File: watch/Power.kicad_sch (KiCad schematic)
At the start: 17 parts, among them IC401 nPM1300-QEXX, X402 Battery

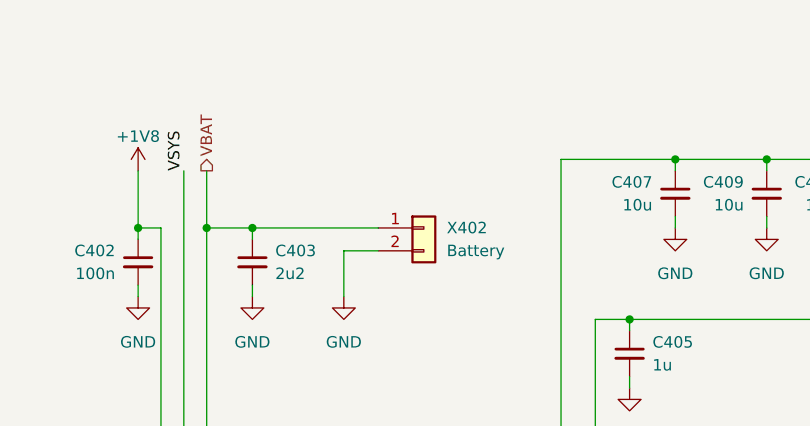
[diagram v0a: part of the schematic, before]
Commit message: Change to a larger battery connector (JST 1.25). Add pads for speaker instead.
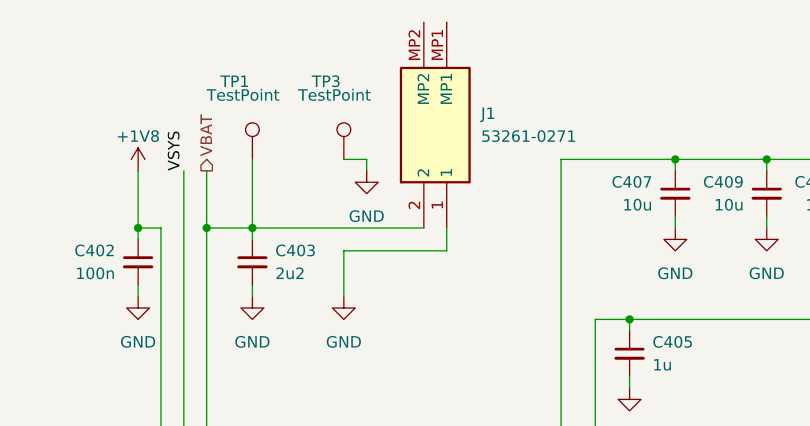
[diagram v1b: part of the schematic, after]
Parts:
- removed X402: Battery, JST_SH_SM02B-SRSS-TB_1x02-1MP_P1.00mm_Horizontal, symbol Connector_Generic:Conn_01x02
- added J1: 53261-0271, ZSWatch:molex_pico, symbol molex_pico:53261-0271
- added TP1, TP3: TestPoint, TestPoint:TestPoint_Loop_D3.50mm_Drill0.9mm_Beaded, symbol Connector:TestPoint
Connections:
- net GND: now also J1.1, TP3.1
- net VBAT: now also J1.2, TP1.1

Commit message: Fix BOM fields, optional speaker flags and connector 3D model
- Rename J1 fields to match the BOM generator
- Exclude optional LS801 from the board and BOM
- Correct the Molex footprint's 3D model reference
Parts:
- J1: Manufacturer_Name Molex -> (none); Manufacturer_Part_Number 53261-0271 -> (none); Mouser Part Number 538-53261-0271 -> (none); manf (none) -> Molex; manf# (none) -> 53261-0271; mouser# (none) -> 538-53261-0271
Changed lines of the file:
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@@
 			)
 		)
-		(property "Mouser Part Number" "538-53261-0271"
+		(property "mouser#" "538-53261-0271"
 			(at 693.04 17.78 0)
 			(effects
@@
 			)
 		)
-		(property "Manufacturer_Name" "Molex"
+		(property "manf" "Molex"
 			(at 893.04 17.78 0)
 			(effects
@@
 			)
 		)
-		(property "Manufacturer_Part_Number" "53261-0271"
+		(property "manf#" "53261-0271"
 			(at 993.04 17.78 0)
 			(effects

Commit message: Make battery/speaker stickout 0.5mm shorter. Add few extra Test Points for power at bottom.
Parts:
- added TP4, TP5, TP6: TestPoint, TestPoint:TestPoint_Pad_D1.0mm, symbol Connector:TestPoint
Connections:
- net +1V8: now also TP4.1
- net +3V0: now also TP5.1
- net VSYS: now also TP6.1
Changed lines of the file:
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@@
 	)
 	(junction
+		(at 252.73 29.21)
+		(diameter 0)
+		(color 0 0 0 0)
+	)
+	(junction
 		(at 231.14 83.82)
 		(diameter 0)
@@
 	)
 	(junction
+		(at 242.57 83.82)
+		(diameter 0)
+		(color 0 0 0 0)
+	)
+	(junction
 		(at 231.14 123.19)
 		(diameter 0)
@@
 		(color 0 0 0 0)
 	)
+	(junction
+		(at 242.57 101.6)
+		(diameter 0)
+		(color 0 0 0 0)
+	)
 	(no_connect
 		(at 137.16 96.52)
@@
 	(wire
 		(pts
+			(xy 242.57 83.82) (xy 251.46 83.82)
+		)
+		(stroke
+			(width 0)
+			(type default)
+		)
+	)
+	(wire
+		(pts
 			(xy 207.01 109.22) (xy 222.25 109.22)
 		)
@@
 	(wire
 		(pts
-			(xy 231.14 83.82) (xy 251.46 83.82)
+			(xy 231.14 83.82) (xy 242.57 83.82)
 		)
 		(stroke
@@
 	(wire
 		(pts
+			(xy 242.57 101.6) (xy 251.46 101.6)
+		)
+		(stroke
+			(width 0)
+			(type default)
+		)
+	)
+	(wire
+		(pts
 			(xy 226.06 29.21) (xy 213.36 29.21)
 		)
@@
 	(wire
 		(pts
-			(xy 246.38 29.21) (xy 264.16 29.21)
+			(xy 246.38 29.21) (xy 252.73 29.21)
 		)
 		(stroke
@@
 	(wire
 		(pts
-			(xy 222.25 101.6) (xy 251.46 101.6)
+			(xy 222.25 101.6) (xy 242.57 101.6)
 		)
 		(stroke
@@
 	(wire
 		(pts
+			(xy 252.73 29.21) (xy 264.16 29.21)
+		)
+		(stroke
+			(width 0)
+			(type default)
+		)
+	)
+	(wire
+		(pts
 			(xy 231.14 121.92) (xy 231.14 123.19)
 		)
@@
 	)
 	(symbol
+		(lib_id "Connector:TestPoint")
+		(at 252.73 29.21 0)
+		(unit 1)
+		(exclude_from_sim no)
+		(in_bom yes)
+		(on_board yes)
+		(dnp no)
+		(property "Reference" "TP6"
+			(at 249.174 20.574 0)
+			(effects
+				(font
+					(size 1.27 1.27)
+				)
+				(justify left)
+			)
+		)
+		(property "Value" "TestPoint"
+			(at 247.65 22.098 0)
+			(effects
+				(font
+					(size 1.27 1.27)
+				)
+				(justify left)
+			)
+		)
+		(property "Footprint" "TestPoint:TestPoint_Pad_D1.0mm"
+			(at 257.81 29.21 0)
+			(effects
+				(font
+					(size 1.27 1.27)
+				)
+				(hide yes)
+			)
+		)
+		(property "Datasheet" "~"
+			(at 257.81 29.21 0)
+			(effects
+				(font
+					(size 1.27 1.27)
+				)
+				(hide yes)
+			)
+		)
+		(property "Description" "test point"
+			(at 252.73 29.21 0)
+			(effects
+				(font
+					(size 1.27 1.27)
+				)
+				(hide yes)
+			)
+		)
+		(pin "1"
+		)
+		(instances
+			(project "ZSWatch-Watch"
+				(path "/d5742f03-3b1a-42e5-a384-018bd4b919aa/c5103ceb-5325-4a84-a025-9638a412984e/cee9a3a2-28cd-4e6c-b23d-337f115f39e8"
+					(reference "TP6")
+					(unit 1)
+				)
+			)
+		)
+	)
+	(symbol
 		(lib_id "Device:C_Small")
 		(at 143.51 46.99 0)
@@
 	)
 	(symbol
+		(lib_id "Connector:TestPoint")
+		(at 242.57 101.6 0)
+		(unit 1)
+		(exclude_from_sim no)
+		(in_bom yes)
+		(on_board yes)
+		(dnp no)
+		(property "Reference" "TP5"
+			(at 239.014 92.964 0)
+			(effects
+				(font
+					(size 1.27 1.27)
+				)
+				(justify left)
+			)
+		)
+		(property "Value" "TestPoint"
+			(at 237.49 94.488 0)
+			(effects
+				(font
+					(size 1.27 1.27)
+				)
+				(justify left)
+			)
+		)
+		(property "Footprint" "TestPoint:TestPoint_Pad_D1.0mm"
+			(at 247.65 101.6 0)
+			(effects
+				(font
+					(size 1.27 1.27)
+				)
+				(hide yes)
+			)
+		)
+		(property "Datasheet" "~"
+			(at 247.65 101.6 0)
+			(effects
+				(font
+					(size 1.27 1.27)
+				)
+				(hide yes)
+			)
+		)
+		(property "Description" "test point"
+			(at 242.57 101.6 0)
+			(effects
+				(font
+					(size 1.27 1.27)
+				)
+				(hide yes)
+			)
+		)
+		(pin "1"
+		)
+		(instances
+			(project "ZSWatch-Watch"
+				(path "/d5742f03-3b1a-42e5-a384-018bd4b919aa/c5103ceb-5325-4a84-a025-9638a412984e/cee9a3a2-28cd-4e6c-b23d-337f115f39e8"
+					(reference "TP5")
+					(unit 1)
+				)
+			)
+		)
+	)
+	(symbol
 		(lib_id "power:GND")
 		(at 220.98 54.61 0)
@@
 					(unit 1)
 				)
+			)
+		)
+	)
+	(symbol
+		(lib_id "Connector:TestPoint")
+		(at 242.57 83.82 0)
+		(unit 1)
+		(exclude_from_sim no)
+		(in_bom yes)
+		(on_board yes)
+		(dnp no)
+		(property "Reference" "TP4"
+			(at 239.014 75.184 0)
+			(effects
+				(font
+					(size 1.27 1.27)
+				)
+				(justify left)
+			)
+		)
+		(property "Value" "TestPoint"
+			(at 237.49 76.708 0)
+			(effects
+				(font
+					(size 1.27 1.27)
+				)
+				(justify left)
+			)
+		)
+		(property "Footprint" "TestPoint:TestPoint_Pad_D1.0mm"
+			(at 247.65 83.82 0)
+			(effects
+				(font
+					(size 1.27 1.27)
+				)
+				(hide yes)
+			)
+		)
+		(property "Datasheet" "~"
+			(at 247.65 83.82 0)
+			(effects
+				(font
+					(size 1.27 1.27)
+				)
+				(hide yes)
+			)
+		)
+		(property "Description" "test point"
+			(at 242.57 83.82 0)
+			(effects
+				(font
+					(size 1.27 1.27)
+				)
+				(hide yes)
+			)
+		)
+		(pin "1"
+		)
+		(instances
+			(project "ZSWatch-Watch"
+				(path "/d5742f03-3b1a-42e5-a384-018bd4b919aa/c5103ceb-5325-4a84-a025-9638a412984e/cee9a3a2-28cd-4e6c-b23d-337f115f39e8"
+					(reference "TP4")
+					(unit 1)
+				)
